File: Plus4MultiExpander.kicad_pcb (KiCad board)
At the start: 2 copper layers, 62.2 x 99.9 mm, 14 parts, among them CN1 EDGE_CONN, CN2 C16_NEWSTYLE_EXP_PORT_1, CN3 C16_NEWSTYLE_EXP_PORT_2, CN4 C16_NEWSTYLE_EXP_PORT_3, U1 74HCT245, U2 74HCT245, U3 74HCT00

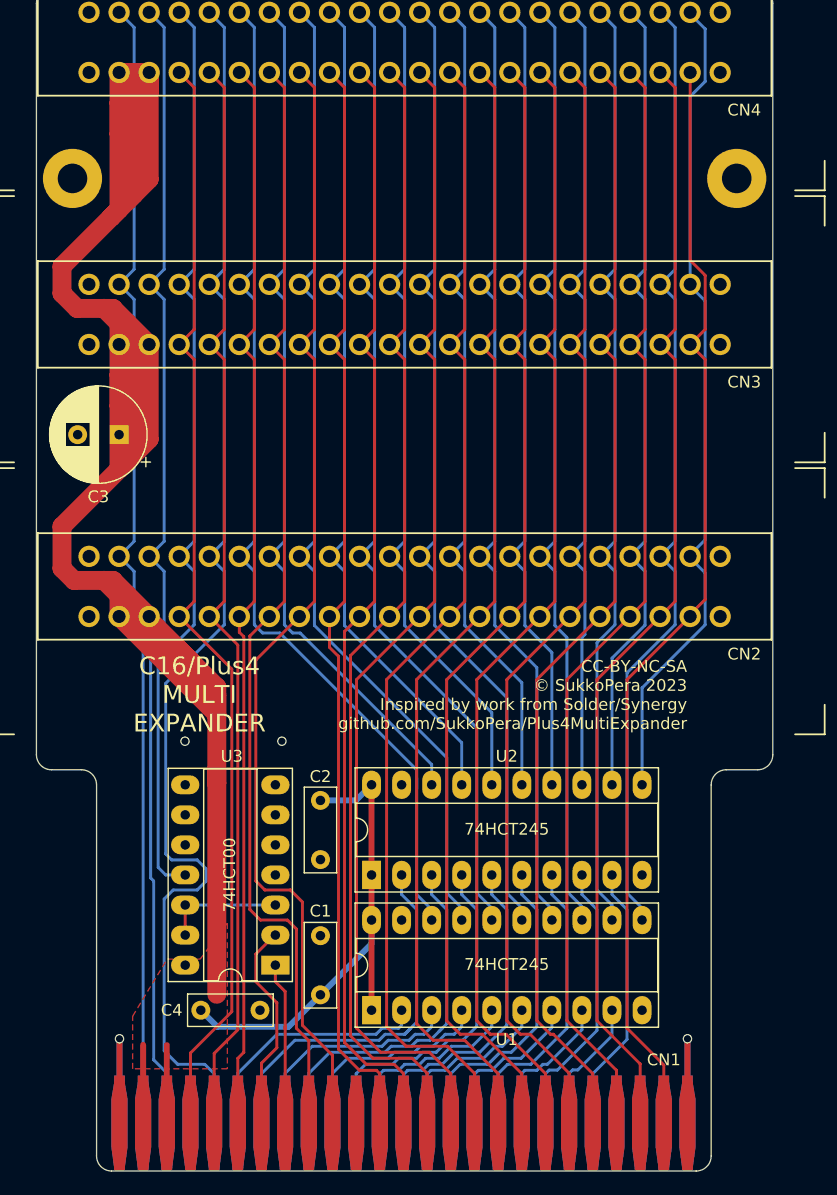
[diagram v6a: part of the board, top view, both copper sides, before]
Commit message: Add mixing resistors for EXT_AUDIO
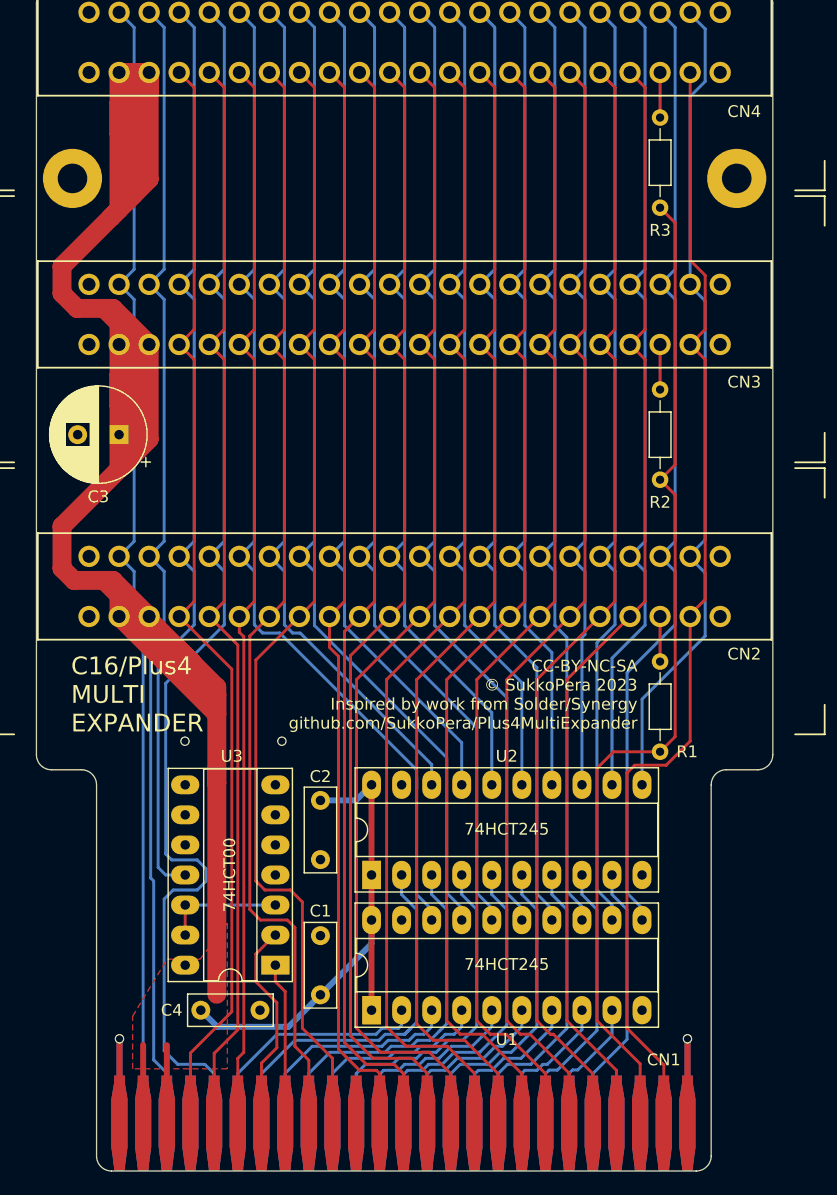
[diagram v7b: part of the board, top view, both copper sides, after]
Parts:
- added R1: 1k, Resistor_THT:R_Axial_DIN0204_L3.6mm_D1.6mm_P7.62mm_Horizontal, F.Cu at (173.9, 105.0)
- added R2: 1k, Resistor_THT:R_Axial_DIN0204_L3.6mm_D1.6mm_P7.62mm_Horizontal, F.Cu at (173.9, 82.0)
- added R3: 1k, Resistor_THT:R_Axial_DIN0204_L3.6mm_D1.6mm_P7.62mm_Horizontal, F.Cu at (173.9, 59.1)
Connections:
- CN2 pad 20: /ext_audio -> Net-(CN2-Pad20)
- CN3 pad 20: /ext_audio -> Net-(CN3-Pad20)
- CN4 pad 20: /ext_audio -> Net-(CN4-Pad20)
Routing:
- net /ext_audio: track 94.6 -> 85.5 mm
- net Net-(CN4-Pad20): track 0.00 -> 3.81 mm
- net Net-(CN3-Pad20): track 0.00 -> 3.81 mm
- net Net-(CN2-Pad20): track 0.00 -> 3.81 mm
- net /phi2: track 94.4 -> 95.9 mm
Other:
- board text added: "V1"

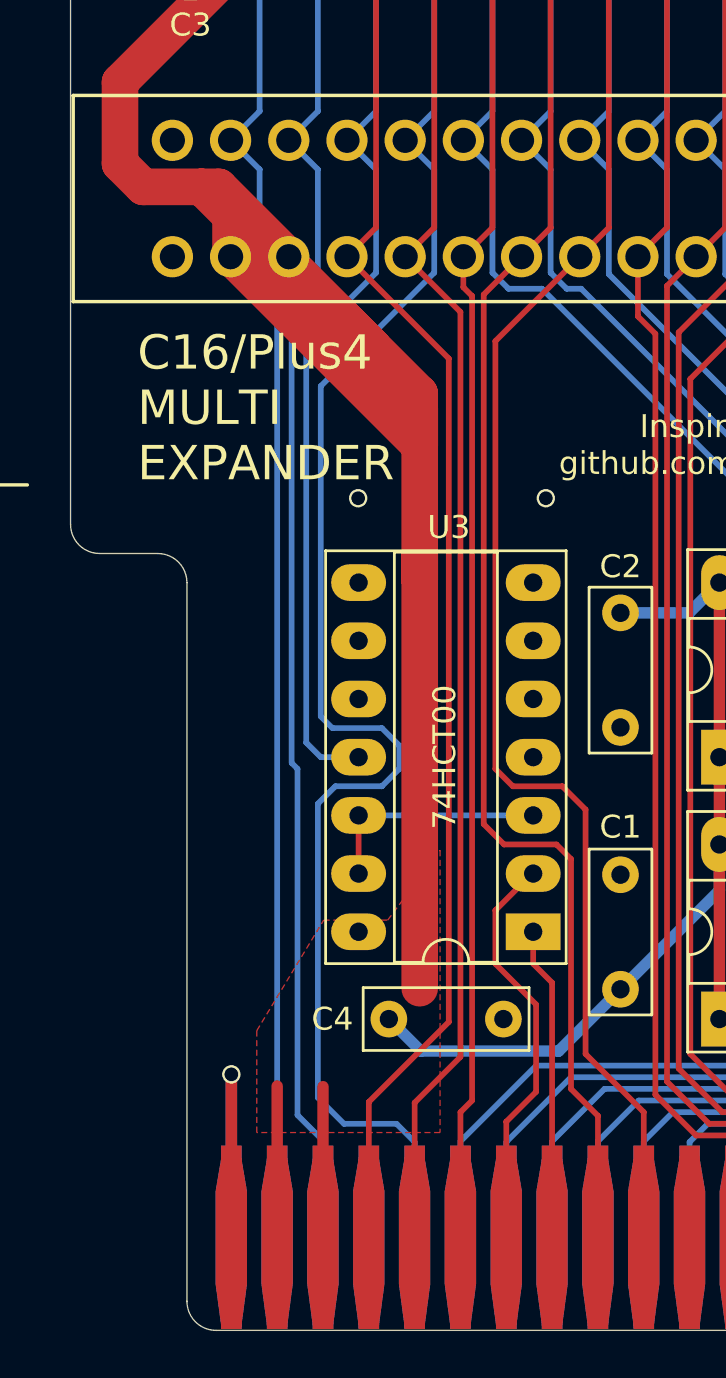
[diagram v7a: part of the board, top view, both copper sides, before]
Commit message: Switch to AND gate and buffer some more signals
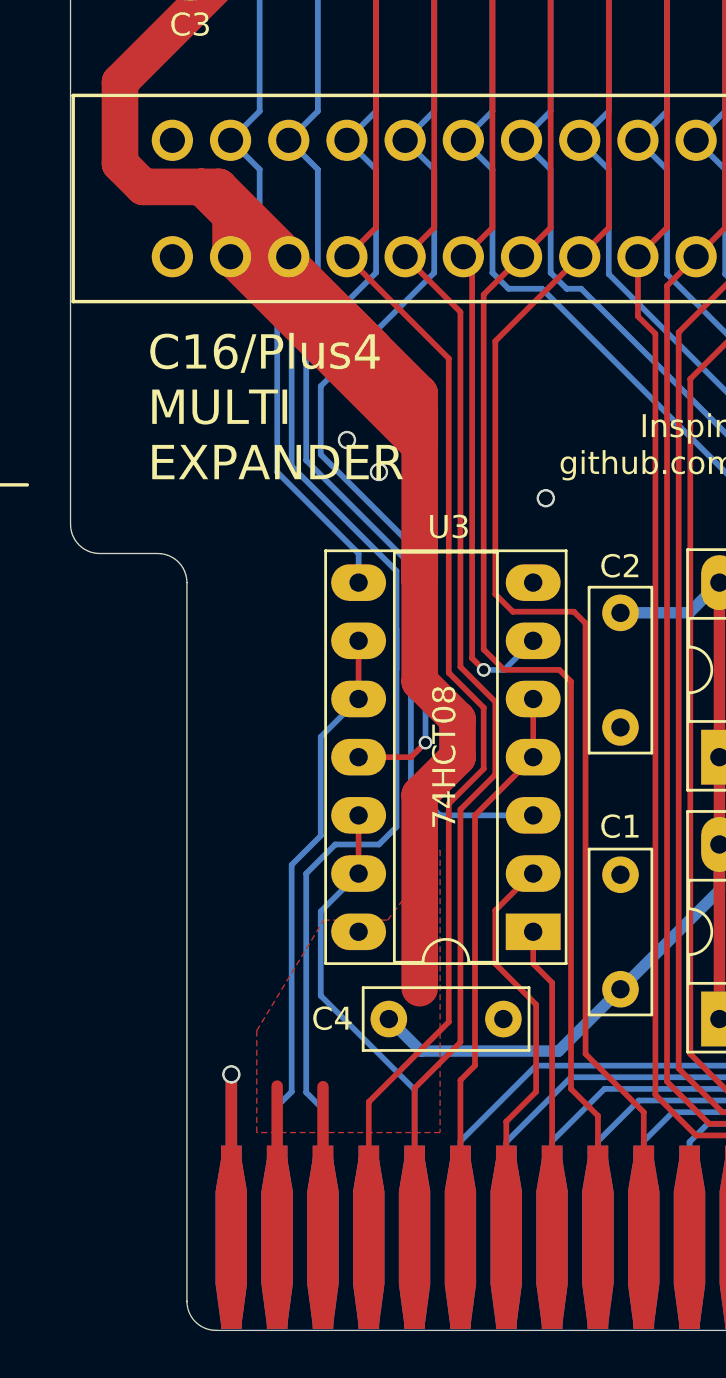
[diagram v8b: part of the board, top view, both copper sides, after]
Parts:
- U3: value 74HCT00 -> 74HCT08
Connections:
- CN1 pad 6: /~c1hi -> /~c1hi_in
- CN1 pad B: /~c1lo -> /~c1lo_in
- CN1 pad E: /phi0 -> /phi0_in
- U3 pad 10: GND -> /~c1lo_in
- U3 pad 11: /~c2 -> /phi0
- U3 pad 12: Net-(U3-Pad12) -> /phi0_in
- U3 pad 13: Net-(U3-Pad12) -> /phi0_in
- U3 pad 3: Net-(U3-Pad12) -> /~c2
- U3 pad 4: GND -> /~c1hi_in
- U3 pad 5: GND -> /~c1hi_in
- U3 pad 6: Net-(U3-Pad6) -> /~c1hi
- U3 pad 8: Net-(U3-Pad8) -> /~c1lo
- U3 pad 9: GND -> /~c1lo_in
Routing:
- net /phi0: track 111.0 -> 82.0 mm, vias 0 -> 1
- net /~c1lo_in: track 0.00 -> 27.5 mm
- net /~c1lo: track 96.8 -> 69.7 mm
- net /~c1hi_in: track 0.00 -> 24.8 mm
- net /~c1hi: track 91.2 -> 69.2 mm, vias 0 -> 1
- net /phi0_in: track 0.00 -> 20.8 mm
- net Net-(U3-Pad12): track 10.2 -> 0.00 mm
- net /~c2: track 78.7 -> 85.8 mm
- net /~reset: track 97.5 -> 103.7 mm
- net +5V: track 254.0 -> 255.4 mm
- net /~irq: track 94.2 -> 95.4 mm
- net /r_~w: track 92.7 -> 94.0 mm
- net GND: vias 4 -> 5
